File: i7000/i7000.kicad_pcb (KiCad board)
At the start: 2 copper layers, 53 parts, among them CN04 Conn_02x30_Counter_Clockwise, CN05 Conn_02x07_Counter_Clockwise

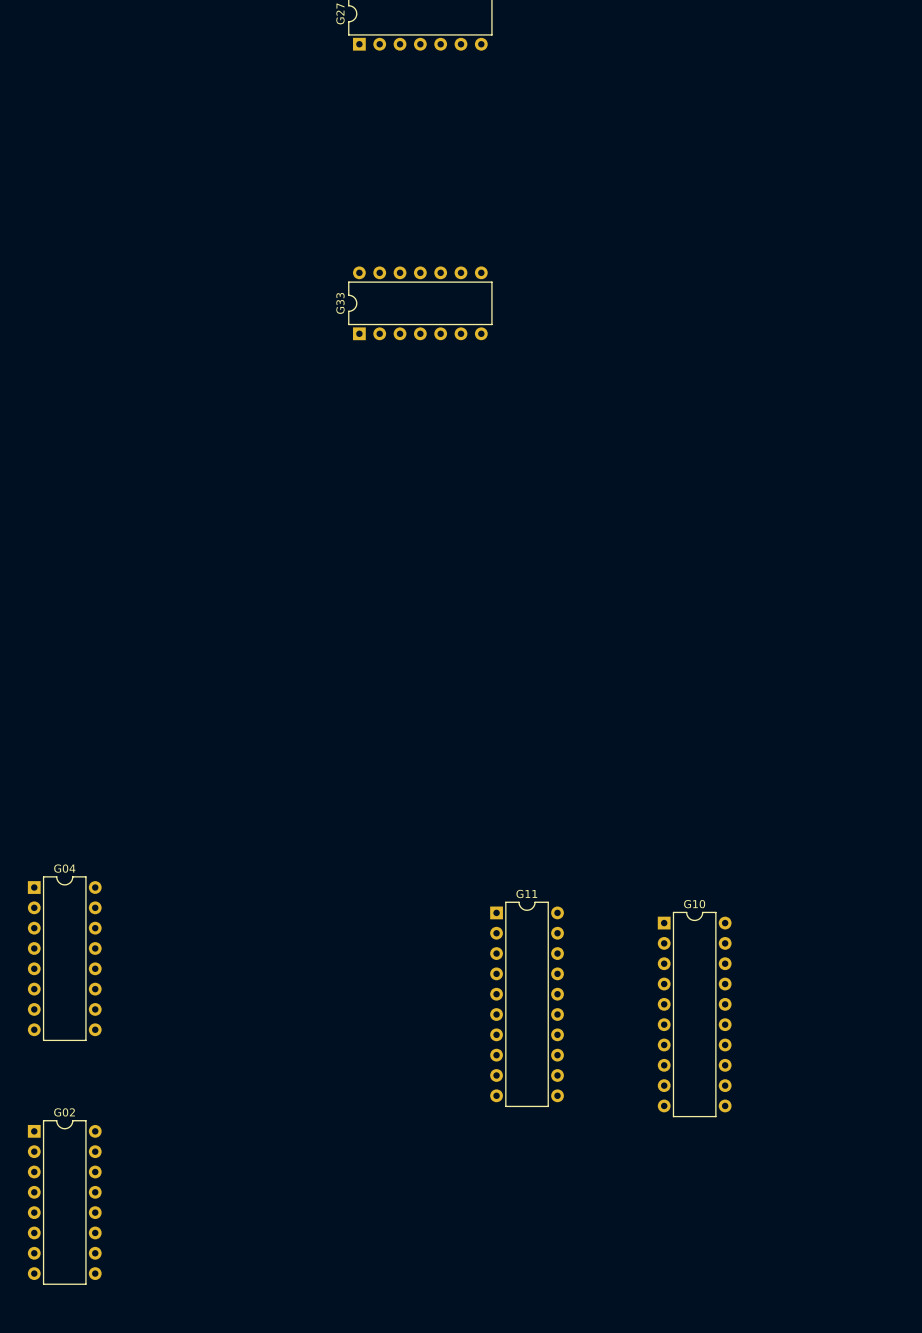
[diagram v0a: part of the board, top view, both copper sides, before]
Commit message: atualizando footprints no layout da PCB
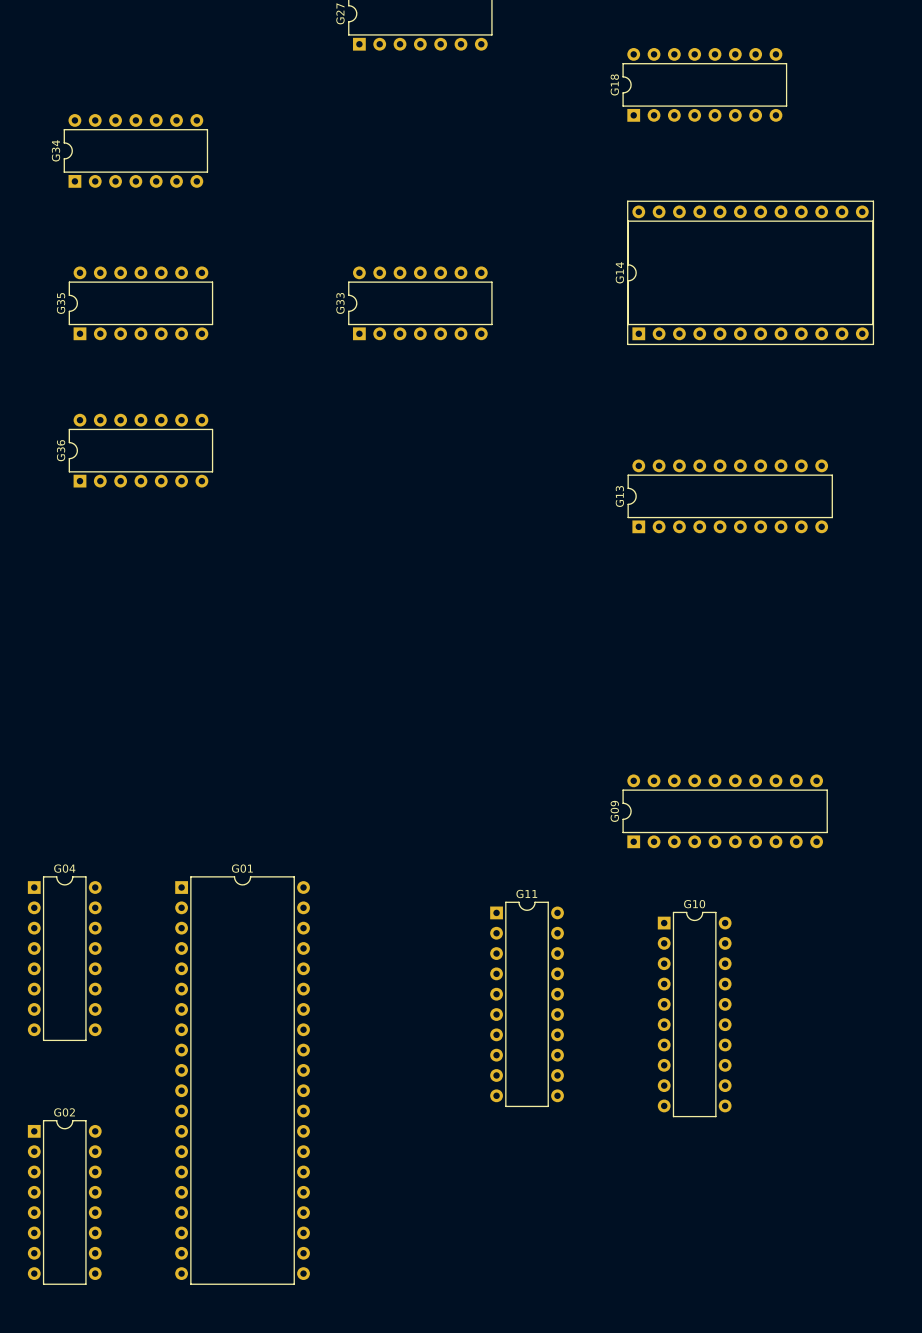
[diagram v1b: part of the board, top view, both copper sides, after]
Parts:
- added G01: MC6845, Housings_DIP:DIP-40_W15.24mm, F.Cu at (333.4, 294.6)
- added G09: 74LS273, Housings_DIP:DIP-20_W7.62mm, F.Cu at (389.9, 288.9)
- added G13: 74LS244, Housings_DIP:DIP-20_W7.62mm, F.Cu at (390.5, 249.6)
- added G14: 2732, Housings_DIP:DIP-24_W15.24mm_Socket, F.Cu at (390.5, 225.4)
- added G18: 74LS166, Housings_DIP:DIP-16_W7.62mm, F.Cu at (389.9, 198.1)
- added G34: 74LS32, Housings_DIP:DIP-14_W7.62mm, F.Cu at (320.0, 206.4)
- added G35: 74LS08, Housings_DIP:DIP-14_W7.62mm, F.Cu at (320.7, 225.4)
- added G36: 74LS86, Housings_DIP:DIP-14_W7.62mm, F.Cu at (320.7, 243.8)
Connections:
- E16 pad 14: Net-(E16-Pad14) -> DRAM_OUT0
- E17 pad 14: Net-(E17-Pad14) -> DRAM_OUT1
- E18 pad 14: Net-(E18-Pad14) -> DRAM_OUT2
- E19 pad 14: Net-(E19-Pad14) -> DRAM_OUT3
- E20 pad 14: Net-(E20-Pad14) -> DRAM_OUT4
- E21 pad 14: Net-(E21-Pad14) -> DRAM_OUT5
- E22 pad 14: Net-(E22-Pad14) -> DRAM_OUT6
- E23 pad 14: Net-(E23-Pad14) -> DRAM_OUT7
- G06 pad 13: Net-(G06-Pad13) -> A11
- G06 pad 14: Net-(G06-Pad14) -> A13
- G06 pad 6: Net-(G06-Pad6) -> GND
- G06 pad 8: Net-(G06-Pad8) -> GND
- G29 pad 10: (no net) -> RA1
- G29 pad 12: (no net) -> RA2
- G29 pad 13: (no net) -> Net-(G29-Pad13)
- G29 pad 8: (no net) -> Net-(G29-Pad8)
- G29 pad 9: (no net) -> RA0

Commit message: update footprints and PCB layout
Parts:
- added G28: 74LS74, Housings_DIP:DIP-14_W7.62mm, F.Cu at (355.6, 207.0)
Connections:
- net Net-(E09-Pad1) renamed ~CPU_RESET_OUT
- CN04 pad 23: Net-(CN04-Pad23) -> RESET_OUT_DELAYED
- E04 pad 3: Net-(E04-Pad3) -> A5
- E29 pad 11: Net-(E29-Pad11) -> Net-(E01-Pad37)
- E29 pad 8: Net-(E29-Pad8) -> RESET_OUT_DELAYED
- G14 pad 20: Net-(G14-Pad20) -> ~CHARGEN_ROM_G
- G27 pad 13: Net-(G27-Pad13) -> ~RESET_OUT_DELAYED
- G27 pad 8: Net-(G27-Pad8) -> Net-(G06-Pad15)
- G27 pad 9: Net-(G27-Pad9) -> ~CHARGEN_ROM_G
- G30 pad 8: (no net) -> ~RESET_OUT_DELAYED
- G30 pad 9: (no net) -> RESET_OUT_DELAYED

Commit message: wip
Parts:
- added G15: 74LS374, Housings_DIP:DIP-20_W7.62mm, F.Cu at (398.8, 358.8)
- added G16: 74LS374, Housings_DIP:DIP-20_W7.62mm, F.Cu at (426.7, 304.8)
- added G17: 74LS374, Housings_DIP:DIP-20_W7.62mm, F.Cu at (447.7, 304.8)
- added G19: Conn_02x08_Counter_Clockwise, Housings_DIP:DIP-16_W7.62mm, F.Cu at (378.5, 358.8)
- added G23: 74LS174, Housings_DIP:DIP-16_W7.62mm, F.Cu at (510.5, 255.3)
- moved G11 6.38 mm to (373.4, 304.2)
- moved G10 5.12 mm to (394.3, 304.2)
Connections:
- G18 pad 13: Net-(G18-Pad13) -> CHARGEN_SERIAL_OUT
- G28 pad 3: Net-(G28-Pad3) -> G28.3
- G29 pad 13: Net-(G29-Pad13) -> REG1_BIT4
- G30 pad 3: (no net) -> Net-(G30-Pad3)
- G30 pad 4: (no net) -> Net-(G30-Pad4)
- G30 pad 5: (no net) -> Net-(G30-Pad4)
- G30 pad 6: (no net) -> G28.3
- G33 pad 1: (no net) -> CHARGEN_SERIAL_OUT
- G33 pad 2: (no net) -> Net-(G33-Pad2)
- G35 pad 1: Net-(G35-Pad1) -> Net-(G33-Pad2)
- G35 pad 2: Net-(G35-Pad2) -> Net-(G29-Pad8)
- G35 pad 4: Net-(G35-Pad4) -> G28.3
- G36 pad 2: Net-(G36-Pad2) -> REG0_BIT2

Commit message: avanços de hoje ;-)
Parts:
- added C207: C, Capacitors_ThroughHole:C_Disc_D3.8mm_W2.6mm_P2.50mm, F.Cu at (165.7, 337.8)
- added C227: C, Capacitors_ThroughHole:C_Disc_D3.8mm_W2.6mm_P2.50mm, F.Cu at (497.2, 218.4)
- added E38: 74LS04, Housings_DIP:DIP-14_W7.62mm, F.Cu at (135.9, 327.0)
- added F20: 74LS02, Housings_DIP:DIP-14_W7.62mm, F.Cu at (438.8, 181.6)
- added G22: 74LS174, Housings_DIP:DIP-16_W7.62mm, F.Cu at (546.7, 45.1)
- added G26: 74LS163, Housings_DIP:DIP-16_W7.62mm, F.Cu at (356.2, 243.2)
- added JP03: Conn_01x03, Pin_Headers:Pin_Header_Straight_1x03_Pitch2.54mm, F.Cu at (492.1, 196.2)
- added JP04: Conn_01x03, Pin_Headers:Pin_Header_Straight_1x03_Pitch2.54mm, F.Cu at (500.4, 196.2)
- added JP05: Conn_01x03, Pin_Headers:Pin_Header_Straight_1x03_Pitch2.54mm, F.Cu at (292.7, 256.5)
- added R29: R, Resistors_ThroughHole:R_Axial_DIN0207_L6.3mm_D2.5mm_P10.16mm_Horizontal, F.Cu at (157.5, 344.8)
- added R38: R, Resistors_ThroughHole:R_Axial_DIN0207_L6.3mm_D2.5mm_P10.16mm_Horizontal, F.Cu at (153.0, 334.6)
- added R82: R, Resistors_ThroughHole:R_Axial_DIN0207_L6.3mm_D2.5mm_P10.16mm_Horizontal, F.Cu at (490.9, 219.1)
- added R83: R, Resistors_ThroughHole:R_Axial_DIN0207_L6.3mm_D2.5mm_P10.16mm_Horizontal, F.Cu at (501.0, 208.3)
- added XTA2: Crystal, Crystals:Crystal_AT310_d3.0mm_l10.0mm_Horizontal_1EP_style2, F.Cu at (148.6, 334.0)
- added XTA3: Crystal, Crystals:Crystal_AT310_d3.0mm_l10.0mm_Horizontal_1EP_style2, F.Cu at (504.3, 207.6)
- added XTA4: Crystal, Crystals:Crystal_AT310_d3.0mm_l10.0mm_Horizontal_1EP_style2, F.Cu at (485.8, 197.5)
- moved G23 17.6 mm to (493.4, 251.5)
- moved G30 17.6 mm to (492.1, 233.7)
- moved E27 13.7 mm to (147.3, 152.4)
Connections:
- net G28.3 renamed G30.6_CLK
- net Net-(F02-Pad13) renamed F17.9_MC1488
- net Net-(F02-Pad17) renamed F17.2_MC1488
- net REG0_BIT2 renamed FF_23.2
- E01 pad 23: Net-(E01-Pad23) -> ~CPU_RSTB
- E27 pad 1: (no net) -> Net-(E27-Pad1)
- E27 pad 2: (no net) -> ~CPU_RSTB
- F01 pad 12: Net-(F01-Pad12) -> D0
- F01 pad 13: Net-(F01-Pad13) -> D1
- F01 pad 14: Net-(F01-Pad14) -> D2
- F01 pad 15: Net-(F01-Pad15) -> D3
- F01 pad 16: Net-(F01-Pad16) -> D4
- F01 pad 17: Net-(F01-Pad17) -> D5
- F01 pad 18: Net-(F01-Pad18) -> D6
- F01 pad 19: Net-(F01-Pad19) -> D7
- F02 pad 1: Net-(F02-Pad1) -> D7
- F02 pad 10: Net-(F02-Pad10) -> Net-(E27-Pad1)
- F02 pad 14: Net-(F02-Pad14) -> Net-(F02-Pad11)
- F02 pad 18: Net-(F02-Pad18) -> Net-(F02-Pad15)
- F02 pad 2: Net-(F02-Pad2) -> D6
- F02 pad 3: Net-(F02-Pad3) -> D5
- F02 pad 4: Net-(F02-Pad4) -> D4
- F02 pad 5: Net-(F02-Pad5) -> D3
- F02 pad 6: Net-(F02-Pad6) -> D2
- F02 pad 7: Net-(F02-Pad7) -> D1
- F02 pad 8: Net-(F02-Pad8) -> D0
- F03 pad 27: Net-(F03-Pad27) -> D7
- F03 pad 28: Net-(F03-Pad28) -> D6
- F03 pad 29: Net-(F03-Pad29) -> D5
- F03 pad 30: Net-(F03-Pad30) -> D4
- F03 pad 31: Net-(F03-Pad31) -> D3
- F03 pad 32: Net-(F03-Pad32) -> D2
- F03 pad 33: Net-(F03-Pad33) -> D1
- F03 pad 34: Net-(F03-Pad34) -> D0
- F04 pad 1: Net-(F04-Pad1) -> D2
- F04 pad 2: Net-(F04-Pad2) -> D3
- F04 pad 27: Net-(F04-Pad27) -> D0
- F04 pad 28: Net-(F04-Pad28) -> D1
- F04 pad 5: Net-(F04-Pad5) -> D4
- F04 pad 6: Net-(F04-Pad6) -> D5
- F04 pad 7: Net-(F04-Pad7) -> D6
- F04 pad 8: Net-(F04-Pad8) -> D7
- F07 pad 15: Net-(F07-Pad15) -> TOGGLE_FF_G27A
- G15 pad 1: Net-(G15-Pad1) -> ~CHARGEN_ROM_G
- G27 pad 1: (no net) -> ~RESET_OUT_DELAYED
- G27 pad 12: Net-(G27-Pad12) -> D0
- G27 pad 2: (no net) -> Net-(G27-Pad2)
- G27 pad 3: (no net) -> TOGGLE_FF_G27A
- G27 pad 4: (no net) -> Net-(G27-Pad4)
- G27 pad 5: (no net) -> Net-(G27-Pad5)
- G27 pad 6: (no net) -> Net-(G27-Pad2)
- G28 pad 12: Net-(G28-Pad12) -> Net-(G27-Pad10)
- G30 pad 1: (no net) -> Net-(G30-Pad1)
- G30 pad 2: (no net) -> Net-(C227-Pad2)
- G34 pad 2: Net-(G34-Pad2) -> F20.1_CLK
- G35 pad 11: (no net) -> Net-(F20-Pad3)
- G35 pad 12: (no net) -> Net-(G28-Pad5)
- G35 pad 13: (no net) -> Net-(G27-Pad2)
- G36 pad 5: Net-(G36-Pad5) -> F20.1_CLK

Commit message: symbol drawing for TMM2016AP (SRAM)
and added a few more symbols on the schematics
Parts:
- moved G22 322.0 mm to (471.2, 358.1)

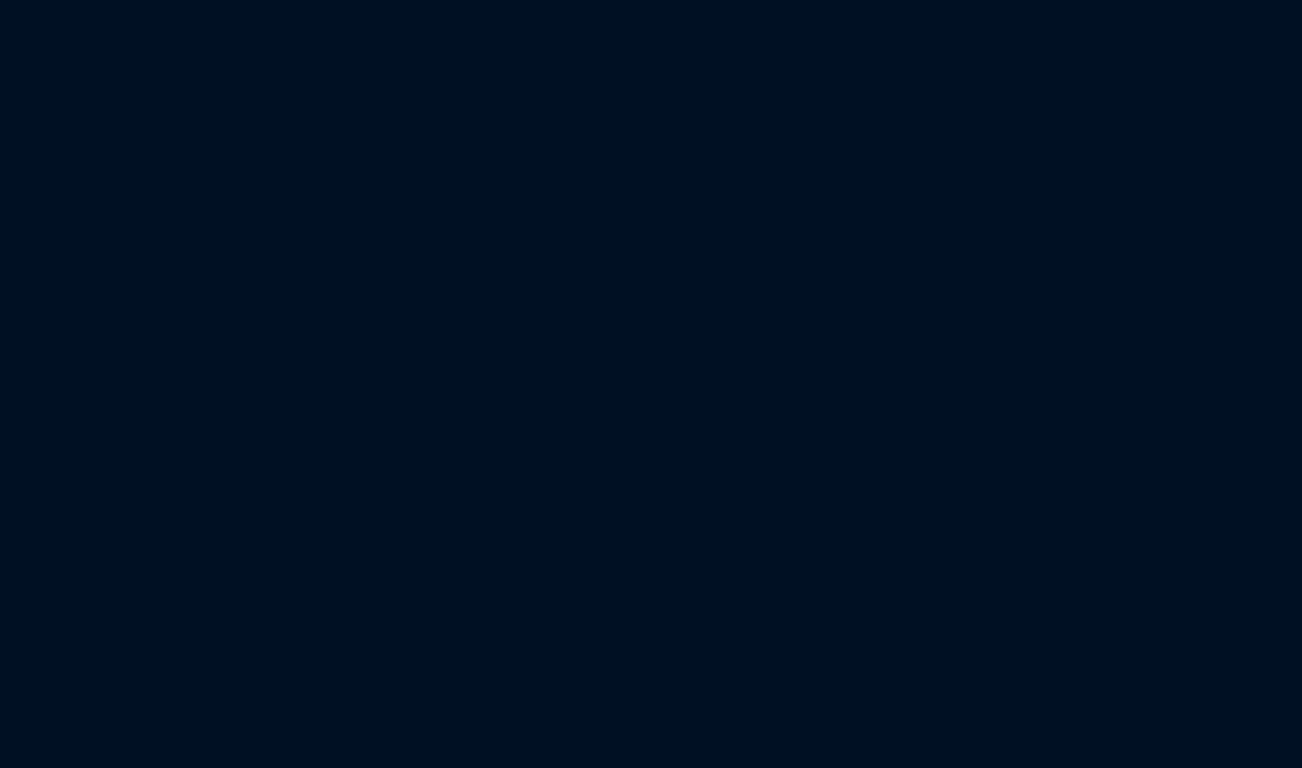
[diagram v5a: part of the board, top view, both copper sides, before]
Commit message: use Package_DIP footprints instead of the older ones called Housings_DIP
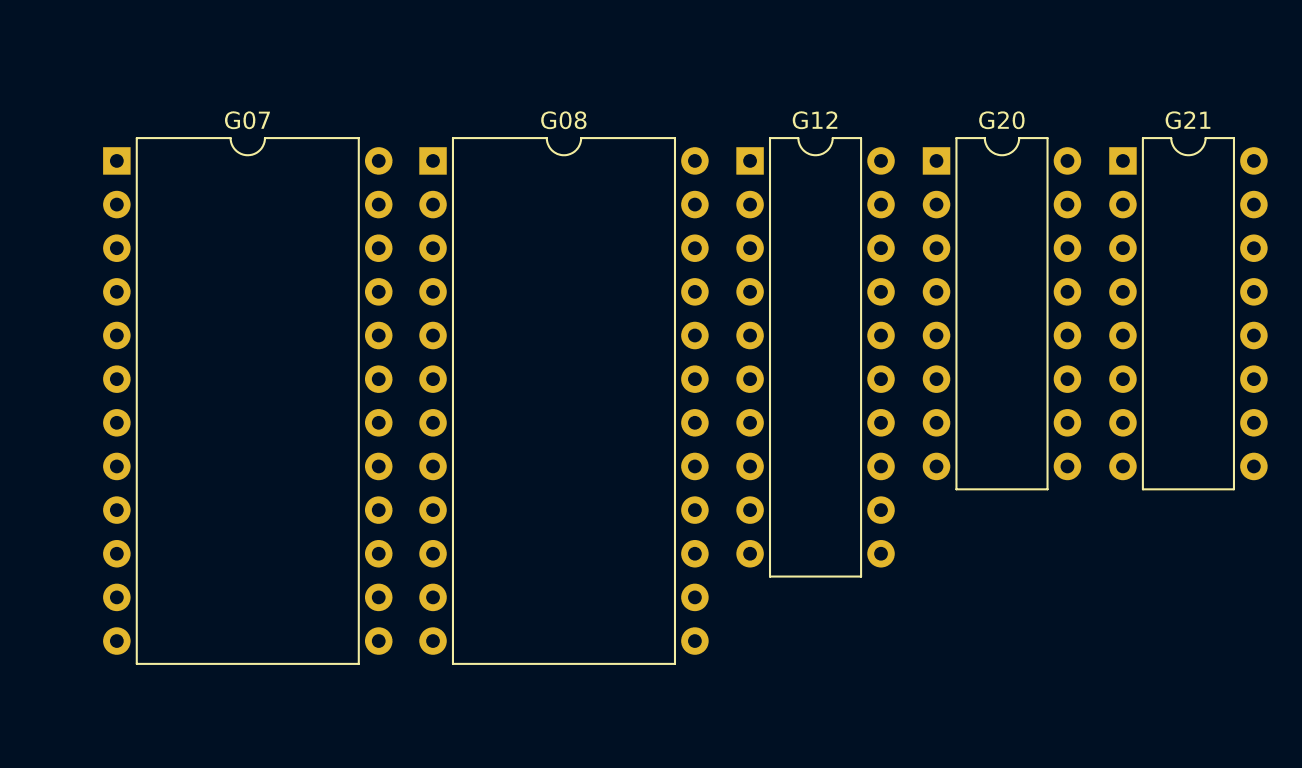
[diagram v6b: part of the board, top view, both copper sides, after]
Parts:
- added G07: TMM2016AP, Package_DIP:DIP-24_W15.24mm, F.Cu at (566.4, 229.9)
- added G08: TMM2016AP, Package_DIP:DIP-24_W15.24mm, F.Cu at (584.8, 229.9)
- added G12: 74LS273, Package_DIP:DIP-20_W7.62mm, F.Cu at (603.3, 229.9)
- added G20: 74LS153, Package_DIP:DIP-16_W7.62mm, F.Cu at (614.1, 229.9)
- added G21: 74LS153, Package_DIP:DIP-16_W7.62mm, F.Cu at (625.0, 229.9)
- CN05: footprint Housings_DIP:DIP-14_W7.62mm_Socket -> Package_DIP:DIP-14_W7.62mm_Socket
- E01, E02, F01, F03, G01: footprint Housings_DIP:DIP-40_W15.24mm -> Package_DIP:DIP-40_W15.24mm
- E03, F04: footprint Housings_DIP:DIP-28_W15.24mm -> Package_DIP:DIP-28_W15.24mm
- E04, G14: footprint Housings_DIP:DIP-24_W15.24mm_Socket -> Package_DIP:DIP-24_W15.24mm_Socket
- E05, E06, E07, E09, E10, E15, G09, G10, G11, G13, G15, G16, G17: footprint Housings_DIP:DIP-20_W7.62mm -> Package_DIP:DIP-20_W7.62mm
- E08, E11, E12, E13, E14, E16, E17, E18, E19, E20, E21, E22, E23, F07, F13, G02, G03, G04, G05, G06, G18, G19, G22, G23, G26: footprint Housings_DIP:DIP-16_W7.62mm -> Package_DIP:DIP-16_W7.62mm
- E26, E27, E28, E29, E32, E36, E38, F14, F15, F16, F20, G27, G28, G29, G30, G31, G32, G33, G34, G35, G36: footprint Housings_DIP:DIP-14_W7.62mm -> Package_DIP:DIP-14_W7.62mm
- F02: footprint Housings_DIP:DIP-24_W15.24mm -> Package_DIP:DIP-24_W15.24mm

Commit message: a few more chips
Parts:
- added F05: ADC0808, Package_DIP:DIP-28_W15.24mm, F.Cu at (492.8, 289.6)
- added G37: 74128, Package_DIP:DIP-14_W7.62mm, F.Cu at (504.2, 341.6)
- added G38: 74LS00, Package_DIP:DIP-14_W7.62mm, F.Cu at (467.4, 341.6)
- added G39: 74LS00, Package_DIP:DIP-14_W7.62mm, F.Cu at (488.9, 355.6)
- added G40: 74S140, Package_DIP:DIP-14_W7.62mm, F.Cu at (504.2, 358.1)
- added G41: 74S140, Package_DIP:DIP-14_W7.62mm, F.Cu at (504.2, 374.6)
- moved G08 327.7 mm to (290.8, 374.6), turned to 90 degrees
- moved G07 280.2 mm to (290.8, 280.7), turned to 90 degrees
- moved G12 279.5 mm to (355.6, 359.4)
- moved G20 242.3 mm to (426.7, 383.5), turned to 90 degrees
- moved G21 239.6 mm to (426.7, 364.5), turned to 90 degrees
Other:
- board text added: "G24"

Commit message: coloquei todos os chips no esquemático e na PCB. Agora falta "só" mapear os sinais...
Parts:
- added E24: 74LS74, Package_DIP:DIP-14_W7.62mm, F.Cu at (124.5, 52.1)
- added E25: 74LS74, Package_DIP:DIP-14_W7.62mm, F.Cu at (63.0, 47.0)
- added E30: 74LS02, Package_DIP:DIP-14_W7.62mm, F.Cu at (92.0, 47.0)
- added E31: 74LS08, Package_DIP:DIP-14_W7.62mm, F.Cu at (92.0, 21.0)
- added E33: 74LS32, Package_DIP:DIP-14_W7.62mm, F.Cu at (34.0, 70.0)
- added E34: 74LS08, Package_DIP:DIP-14_W7.62mm, F.Cu at (34.0, 47.0)
- added E35: 74LS00, Package_DIP:DIP-14_W7.62mm, F.Cu at (34.0, 21.0)
- added E37: SN74LS07N, Package_DIP:DIP-14_W7.62mm, F.Cu at (92.0, 70.0)
- added F06: 74LS138, Package_DIP:DIP-16_W7.62mm, F.Cu at (195.6, 76.2)
- added F08: 74LS74, Package_DIP:DIP-14_W7.62mm, F.Cu at (219.7, 119.4)
- added F10: 74LS163, Package_DIP:DIP-16_W7.62mm, F.Cu at (180.3, 135.9)
- added F11: 74LS74, Package_DIP:DIP-14_W7.62mm, F.Cu at (149.9, 124.5)
- added F12: 74LS74, Package_DIP:DIP-14_W7.62mm, F.Cu at (149.9, 97.8)
- added F17: MC1488, Package_DIP:DIP-14_W7.62mm, F.Cu at (358.1, 25.4)
- added F18: MC1489, Package_DIP:DIP-14_W7.62mm, F.Cu at (358.1, 40.6)
- added F19: MC1489, Package_DIP:DIP-14_W7.62mm, F.Cu at (358.1, 54.6)
- added F21: 74LS04, Package_DIP:DIP-14_W7.62mm, F.Cu at (180.3, 119.4)
- added F22: SN74LS07N, Package_DIP:DIP-14_W7.62mm, F.Cu at (359.4, 94.0)
- added F23: SN74LS07N, Package_DIP:DIP-14_W7.62mm, F.Cu at (359.4, 108.5)
- added F9: 74LS163, Package_DIP:DIP-16_W7.62mm, F.Cu at (180.3, 154.9)
- added G25: 74LS74, Package_DIP:DIP-14_W7.62mm, F.Cu at (257.8, 193.0)
- moved E23 139.4 mm to (128.0, 268.0)
- moved CN04 136.5 mm to (168.9, 256.5)
- moved E22 136.4 mm to (115.3, 268.0)
- moved F05 135.9 mm to (384.8, 207.0)
- moved G22 135.9 mm to (363.2, 275.6)
- moved G37 135.9 mm to (396.2, 259.1)
- moved G38 135.9 mm to (359.4, 259.1)
- moved G39 135.9 mm to (381.0, 273.1)
- moved G40 135.9 mm to (396.2, 275.6)
- moved G41 135.9 mm to (396.2, 292.1)
- moved E21 133.5 mm to (102.6, 268.0)
- moved G30 133.1 mm to (386.7, 152.4)
- moved JP03 133.1 mm to (386.7, 114.9)
- moved R82 133.1 mm to (385.4, 137.8)
- moved XTA3 133.1 mm to (398.9, 126.4)
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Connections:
- E26 pad 1: (no net) -> Net-(E26-Pad1)
- E26 pad 2: (no net) -> Net-(E26-Pad2)
- E26 pad 3: (no net) -> Net-(E26-Pad3)
- E26 pad 4: (no net) -> Net-(E26-Pad4)
- E26 pad 5: (no net) -> Net-(E26-Pad5)
- E26 pad 6: (no net) -> Net-(E26-Pad6)
- F02 pad 13: F17.9_MC1488 -> Net-(F02-Pad13)
- F02 pad 17: F17.2_MC1488 -> Net-(F02-Pad17)
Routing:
- net Net-(E26-Pad11): track 0.00 -> 47.9 mm
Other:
- board outline added: 426 x 307 mm
- board text added: "DP01"
